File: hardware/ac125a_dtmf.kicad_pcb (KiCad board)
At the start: 2 copper layers, 120 x 127 mm, 102 parts, among them J1 112-050-113R001, J2 Conn_01x06_Male, J3 USB_B, J4 DB9_Female_MountingHoles, SW1 SW_Push, U1 PIC18F4550-IP, U10 LAA108, U11 LAA108, U12 H11AA1, U13 H11AA1, U14 MAX202, U2 MT8870, U3 MT8870, U4 74HC595, U5 74HC595, U6 LAA108, U7 LAA108, U8 LAA108, U9 LAA108, Y1 3.579545MHZ

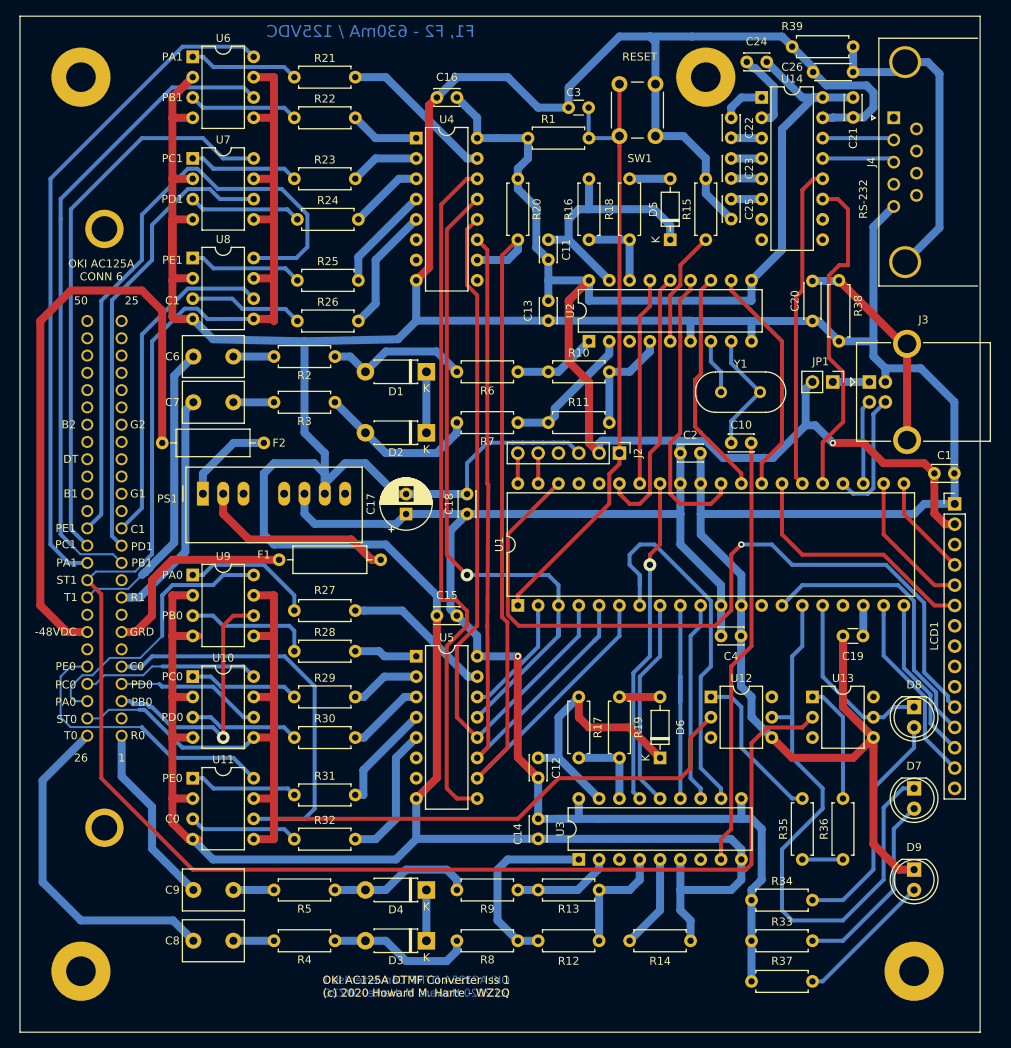
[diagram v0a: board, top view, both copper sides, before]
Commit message: Final schematic and PCB layout for Issue 2.
Corrected errors in Issue 1 and fabbed out the PCB.
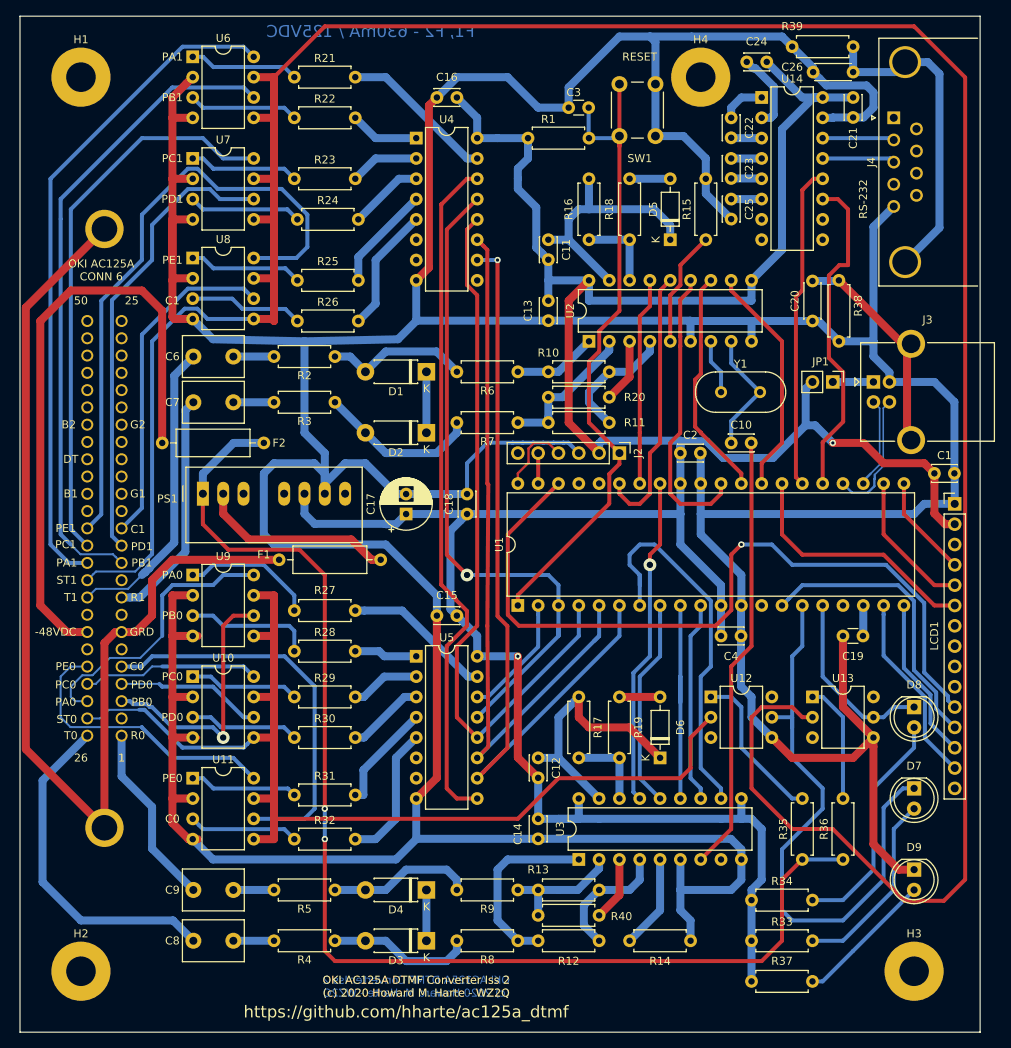
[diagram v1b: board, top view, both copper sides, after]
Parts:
- removed REF** (x4): MountingHole_3.7mm_Pad, MountingHole:MountingHole_3.7mm_Pad
- added H1: MountingHole, MountingHole:MountingHole_3.7mm_Pad, F.Cu at (40.6, 34.3)
- added H2: MountingHole, MountingHole:MountingHole_3.7mm_Pad, F.Cu at (40.6, 146.1)
- added H3: MountingHole, MountingHole:MountingHole_3.7mm_Pad, F.Cu at (144.8, 146.1)
- added H4: MountingHole, MountingHole:MountingHole_3.7mm_Pad, F.Cu at (118.1, 34.3)
- added R40: 220K 1%, Resistor_THT:R_Axial_DIN0207_L6.3mm_D2.5mm_P7.62mm_Horizontal, F.Cu at (105.4, 139.1)
- C3: value NP -> 0.01uF
- C6, C7, C8, C9: value 0.1uF/250V -> 0.01uF/630V
- R1: value 10K -> 4.7K
- R10, R12: value 47K -> 52.3K 1%
- R11, R13: value 47K -> 68.1K 1%
- R2, R3, R4, R5: value 56K -> 110K 1% 1W
- R20: value 1K -> 220K 1%
- R6, R7, R8, R9: value 56K -> 110K 1%
- moved R20 29.6 mm to (106.7, 74.3), turned to 180 degrees
- moved J3 0.51 mm to (139.7, 72.4)
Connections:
- net /Microcontroller/USB_DM renamed /Microcontroller/USB_D-
- net /Microcontroller/USB_DP renamed /Microcontroller/USB_D+
- net AC125A_C0 renamed /AC125A_C0
- net AC125A_C1 renamed /AC125A_C1
- net AC125A_G0 renamed /AC125A_G0
- net AC125A_PA0 renamed /AC125A_PA0
- net AC125A_PA1 renamed /AC125A_PA1
- net AC125A_PB0 renamed /AC125A_PB0
- net AC125A_PB1 renamed /AC125A_PB1
- net AC125A_PC0 renamed /AC125A_PC0
- net AC125A_PC1 renamed /AC125A_PC1
- net AC125A_PD0 renamed /AC125A_PD0
- net AC125A_PD1 renamed /AC125A_PD1
- net AC125A_PE0 renamed /AC125A_PE0
- net AC125A_PE1 renamed /AC125A_PE1
- net AC125A_R1 renamed /AC125A_R1
- F2 pad 1: AC125A_B0 -> /AC125A_B0
- J1 pad 10: Net-(J1-Pad10) -> (no net)
- J1 pad 14: Net-(J1-Pad14) -> (no net)
- J1 pad 15: AC125A_G1 -> (no net)
- J1 pad 16: Net-(J1-Pad16) -> (no net)
- J1 pad 17: Net-(J1-Pad17) -> (no net)
- J1 pad 18: Net-(J1-Pad18) -> (no net)
- J1 pad 19: AC125A_G2 -> (no net)
- J1 pad 2: Net-(J1-Pad2) -> (no net)
- J1 pad 20: Net-(J1-Pad20) -> (no net)
- J1 pad 21: Net-(J1-Pad21) -> (no net)
- J1 pad 22: Net-(J1-Pad22) -> (no net)
- J1 pad 23: Net-(J1-Pad23) -> (no net)
- J1 pad 24: Net-(J1-Pad24) -> (no net)
- J1 pad 25: Net-(J1-Pad25) -> (no net)
- J1 pad 31: Net-(J1-Pad31) -> (no net)
- J1 pad 33: Net-(J1-Pad33) -> (no net)
- J1 pad 39: Net-(J1-Pad39) -> (no net)
- J1 pad 40: AC125A_B1 -> (no net)
- J1 pad 41: Net-(J1-Pad41) -> (no net)
- J1 pad 42: /AC125A_DT -> (no net)
- J1 pad 43: Net-(J1-Pad43) -> (no net)
- J1 pad 44: AC125A_B2 -> (no net)
- J1 pad 45: Net-(J1-Pad45) -> (no net)
- J1 pad 46: Net-(J1-Pad46) -> (no net)
- J1 pad 47: Net-(J1-Pad47) -> (no net)
- J1 pad 48: Net-(J1-Pad48) -> (no net)
- J1 pad 49: Net-(J1-Pad49) -> (no net)
- J1 pad 50: Net-(J1-Pad50) -> (no net)
- J1 pad 6: Net-(J1-Pad6) -> (no net)
- J1 pad 8: Net-(J1-Pad8) -> (no net)
- J1 pad MH1: Net-(J1-PadMH1) -> Net-(F1-Pad1)
- J1 pad MH2: Net-(J1-PadMH2) -> Net-(F1-Pad1)
- J2 pad 4: Net-(J2-Pad4) -> /Microcontroller/ICSP_PGD
- J2 pad 6: /Microcontroller/ICSP_PGD -> (no net)
- J4 pad 1: Net-(J4-Pad1) -> (no net)
- J4 pad 4: Net-(J4-Pad4) -> (no net)
- J4 pad 6: Net-(J4-Pad6) -> (no net)
- J4 pad 7: Net-(J4-Pad7) -> (no net)
- J4 pad 8: Net-(J4-Pad8) -> (no net)
- J4 pad 9: Net-(J4-Pad9) -> (no net)
- LCD1 pad 10: Net-(LCD1-Pad10) -> (no net)
- LCD1 pad 15: Net-(LCD1-Pad15) -> (no net)
- LCD1 pad 3: Net-(LCD1-Pad3) -> (no net)
- LCD1 pad 7: Net-(LCD1-Pad7) -> (no net)
- LCD1 pad 8: Net-(LCD1-Pad8) -> (no net)
- LCD1 pad 9: Net-(LCD1-Pad9) -> (no net)
- PS1 pad 1: AC125A_B0 -> /AC125A_B0
- PS1 pad 3: Net-(PS1-Pad3) -> (no net)
- PS1 pad 5: Net-(PS1-Pad5) -> (no net)
- R20 pad 1: +5V -> Net-(R20-Pad1)
- R20 pad 2: /Microcontroller/SSR_SRCLR_ -> Net-(R11-Pad2)
- R35 pad 1: /Microcontroller/AC125A_B0 -> /AC125A_B0
- R36 pad 1: /Microcontroller/AC125A_B0 -> /AC125A_B0
- U1 pad 13: Net-(U1-Pad13) -> (no net)
- U1 pad 17: Net-(U1-Pad17) -> (no net)
- U1 pad 36: Net-(U1-Pad36) -> (no net)
- U1 pad 37: Net-(U1-Pad37) -> (no net)
- U12 pad 3: Net-(U12-Pad3) -> (no net)
- U12 pad 6: Net-(U12-Pad6) -> (no net)
- U13 pad 3: Net-(U13-Pad3) -> (no net)
- U13 pad 6: Net-(U13-Pad6) -> (no net)
- U14 pad 10: Net-(U14-Pad10) -> (no net)
- U14 pad 7: Net-(U14-Pad7) -> (no net)
- U14 pad 8: Net-(U14-Pad8) -> (no net)
- U14 pad 9: Net-(U14-Pad9) -> (no net)
- U2 pad 3: Net-(U2-Pad3) -> Net-(R20-Pad1)
- U3 pad 7: Net-(U3-Pad7) -> Net-(C10-Pad2)
- U3 pad 8: Net-(C10-Pad2) -> (no net)
- U4 pad 6: Net-(U4-Pad6) -> (no net)
- U4 pad 7: Net-(U4-Pad7) -> (no net)
- U4 pad 9: Net-(U4-Pad9) -> (no net)
- U5 pad 6: Net-(U5-Pad6) -> (no net)
- U5 pad 7: Net-(U5-Pad7) -> (no net)
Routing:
- net /AC125A_B0: track 0.00 -> 155.4 mm, vias 0 -> 2
- net Net-(F1-Pad1): track 26.0 -> 134.8 mm
- net /AC125A_ST1: track 237.9 -> 345.1 mm
- net AC125A_B0: track 11.7 -> 0.00 mm
- net Net-(R40-Pad1): track 0.00 -> 8.04 mm
- net Net-(R20-Pad1): track 0.00 -> 8.04 mm
- net /Microcontroller/SSR_SRCLR_: track 106.1 -> 98.6 mm, vias 0 -> 1
- net /Microcontroller/ICSP_PGD: track 3.81 -> 9.50 mm
- net /Microcontroller/AC125A_B0: track 5.08 -> 0.00 mm
- net /Microcontroller/MCLR: track 78.2 -> 82.6 mm
- net Net-(R13-Pad2): track 12.4 -> 15.6 mm
- net Net-(R10-Pad2): track 13.8 -> 15.9 mm
- net Net-(R11-Pad2): track 17.1 -> 18.8 mm
- net Net-(R12-Pad2): track 14.5 -> 16.1 mm
- net Net-(C10-Pad2): track 53.7 -> 54.7 mm
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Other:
- board text added: "OKI AC125A DTMF Converter Iss 2 (c) 2020 Howard M. Harte - WZ2Q"
- board text added: "https://github.com/hharte/ac125a_dtmf"
- board text removed: "OKI AC125A DTMF Converter Iss 1 (c) 2020 Howard M. Harte - WZ2Q"

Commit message: Update schematic/layout to KiCAD 6.0
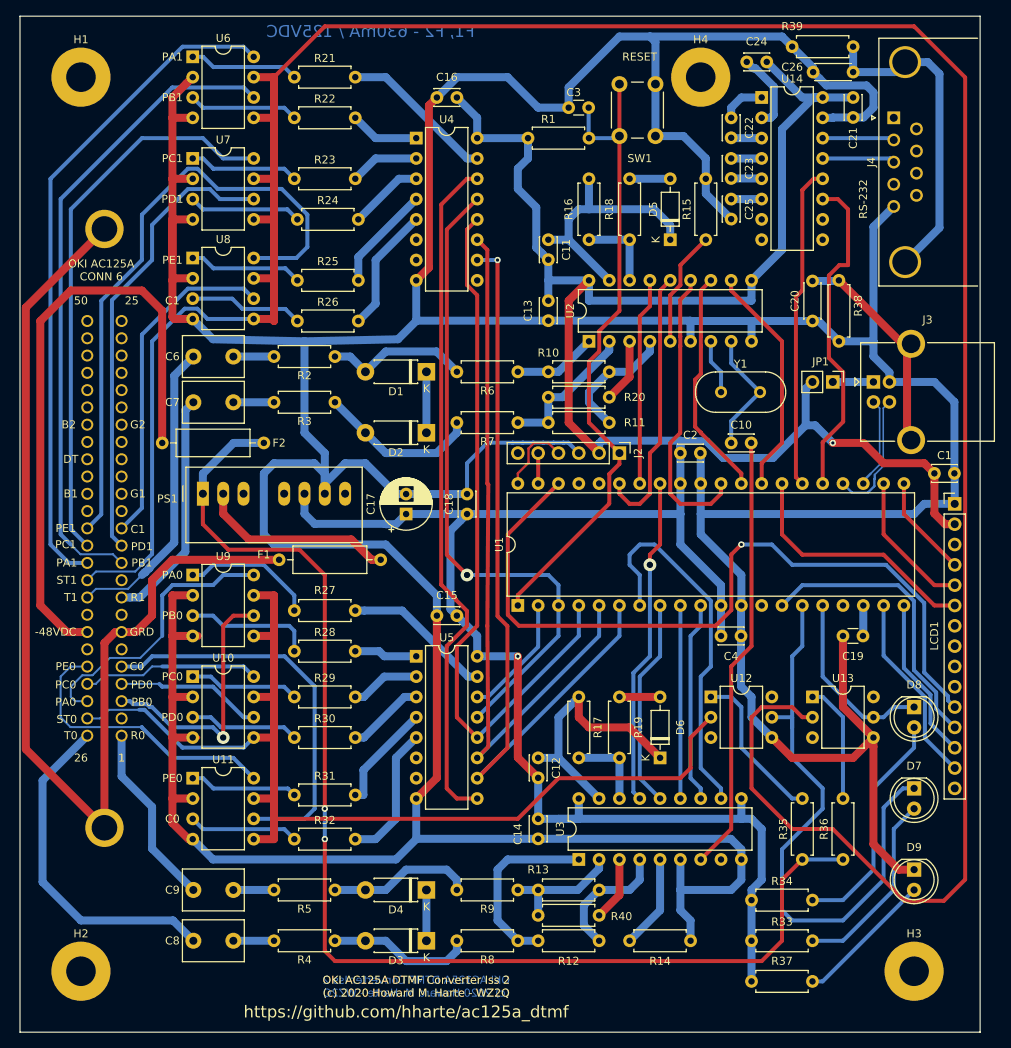
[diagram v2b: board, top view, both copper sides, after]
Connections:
- J1 pad 10: (no net) -> unconnected-(J1-Pad10)
- J1 pad 14: (no net) -> unconnected-(J1-Pad14)
- J1 pad 15: (no net) -> /AC125A_G1
- J1 pad 16: (no net) -> unconnected-(J1-Pad16)
- J1 pad 17: (no net) -> unconnected-(J1-Pad17)
- J1 pad 18: (no net) -> unconnected-(J1-Pad18)
- J1 pad 19: (no net) -> /AC125A_G2
- J1 pad 2: (no net) -> unconnected-(J1-Pad2)
- J1 pad 20: (no net) -> unconnected-(J1-Pad20)
- J1 pad 21: (no net) -> unconnected-(J1-Pad21)
- J1 pad 22: (no net) -> unconnected-(J1-Pad22)
- J1 pad 23: (no net) -> unconnected-(J1-Pad23)
- J1 pad 24: (no net) -> unconnected-(J1-Pad24)
- J1 pad 25: (no net) -> unconnected-(J1-Pad25)
- J1 pad 31: (no net) -> unconnected-(J1-Pad31)
- J1 pad 33: (no net) -> unconnected-(J1-Pad33)
- J1 pad 39: (no net) -> unconnected-(J1-Pad39)
- J1 pad 40: (no net) -> /AC125A_B1
- J1 pad 41: (no net) -> unconnected-(J1-Pad41)
- J1 pad 42: (no net) -> /AC125A_DT
- J1 pad 43: (no net) -> unconnected-(J1-Pad43)
- J1 pad 44: (no net) -> /AC125A_B2
- J1 pad 45: (no net) -> unconnected-(J1-Pad45)
- J1 pad 46: (no net) -> unconnected-(J1-Pad46)
- J1 pad 47: (no net) -> unconnected-(J1-Pad47)
- J1 pad 48: (no net) -> unconnected-(J1-Pad48)
- J1 pad 49: (no net) -> unconnected-(J1-Pad49)
- J1 pad 50: (no net) -> unconnected-(J1-Pad50)
- J1 pad 6: (no net) -> unconnected-(J1-Pad6)
- J1 pad 8: (no net) -> unconnected-(J1-Pad8)
- J2 pad 6: (no net) -> unconnected-(J2-Pad6)
- J4 pad 1: (no net) -> unconnected-(J4-Pad1)
- J4 pad 4: (no net) -> unconnected-(J4-Pad4)
- J4 pad 6: (no net) -> unconnected-(J4-Pad6)
- J4 pad 7: (no net) -> unconnected-(J4-Pad7)
- J4 pad 8: (no net) -> unconnected-(J4-Pad8)
- J4 pad 9: (no net) -> unconnected-(J4-Pad9)
- LCD1 pad 10: (no net) -> unconnected-(LCD1-Pad10)
- LCD1 pad 15: (no net) -> unconnected-(LCD1-Pad15)
- LCD1 pad 3: (no net) -> unconnected-(LCD1-Pad3)
- LCD1 pad 7: (no net) -> unconnected-(LCD1-Pad7)
- LCD1 pad 8: (no net) -> unconnected-(LCD1-Pad8)
- LCD1 pad 9: (no net) -> unconnected-(LCD1-Pad9)
- PS1 pad 3: (no net) -> unconnected-(PS1-Pad3)
- PS1 pad 5: (no net) -> unconnected-(PS1-Pad5)
- U1 pad 13: (no net) -> unconnected-(U1-Pad13)
- U1 pad 17: (no net) -> unconnected-(U1-Pad17)
- U1 pad 36: (no net) -> unconnected-(U1-Pad36)
- U1 pad 37: (no net) -> unconnected-(U1-Pad37)
- U12 pad 3: (no net) -> unconnected-(U12-Pad3)
- U12 pad 6: (no net) -> unconnected-(U12-Pad6)
- U13 pad 3: (no net) -> unconnected-(U13-Pad3)
- U13 pad 6: (no net) -> unconnected-(U13-Pad6)
- U14 pad 10: (no net) -> unconnected-(U14-Pad10)
- U14 pad 7: (no net) -> unconnected-(U14-Pad7)
- U14 pad 8: (no net) -> unconnected-(U14-Pad8)
- U14 pad 9: (no net) -> unconnected-(U14-Pad9)
- U3 pad 8: (no net) -> unconnected-(U3-Pad8)
- U4 pad 6: (no net) -> unconnected-(U4-Pad6)
- U4 pad 7: (no net) -> unconnected-(U4-Pad7)
- U4 pad 9: (no net) -> unconnected-(U4-Pad9)
- U5 pad 6: (no net) -> unconnected-(U5-Pad6)
- U5 pad 7: (no net) -> unconnected-(U5-Pad7)
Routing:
- net /Microcontroller/DTMF0_Q2: track 27.4 -> 24.1 mm
- net GND: track 726.0 -> 724.0 mm
- net /Microcontroller/SSR_OE_: track 83.6 -> 82.3 mm
- net /Microcontroller/DTMF0_Q0: track 48.0 -> 46.8 mm
- net /Microcontroller/MCLR: track 82.6 -> 81.3 mm
- net Net-(R12-Pad1): track 24.2 -> 23.2 mm
- net /Microcontroller/SSR_SRCLK: track 92.2 -> 91.3 mm
- net Net-(R11-Pad2): track 18.8 -> 18.2 mm
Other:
- net class Default removed

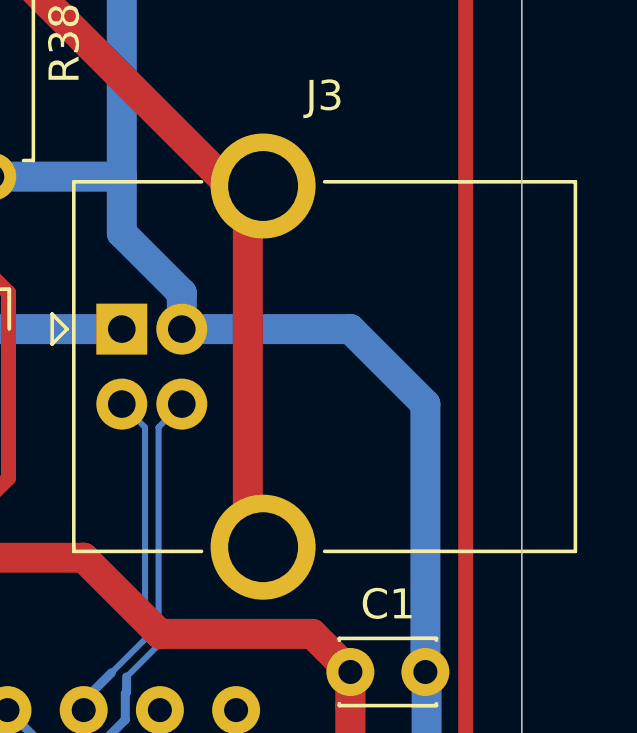
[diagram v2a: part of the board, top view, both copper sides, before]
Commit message: Fix a couple DRC errors in the layout.
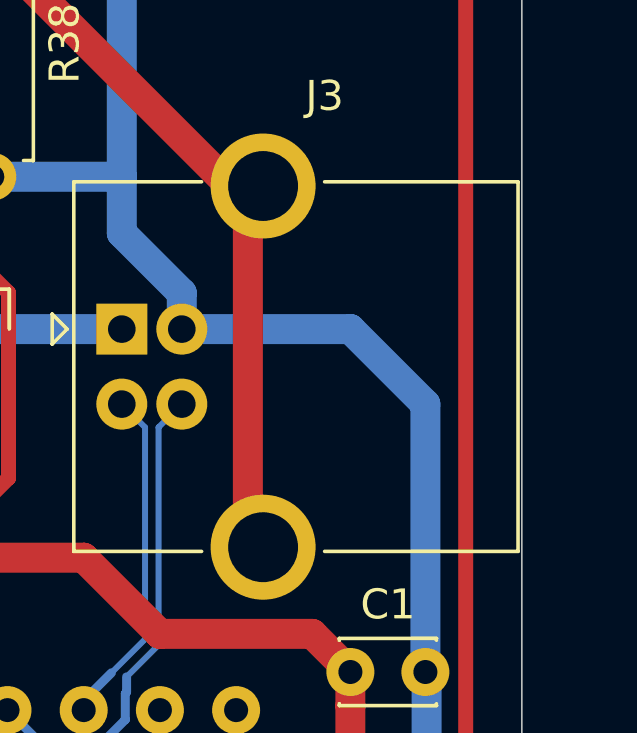
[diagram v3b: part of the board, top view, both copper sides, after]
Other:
- rule pad_to_mask_clearance: 0.051 -> 0
